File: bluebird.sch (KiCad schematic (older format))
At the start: 17 parts

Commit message: Add and wire key matrix, IO expander
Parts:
- added R? (x2): 10k, symbol Device:R
- added U2: MCP23017_SS, Package_SO:SSOP-28_5.3x10.2mm_P0.65mm, symbol Interface_Expansion:MCP23017_SS
- U1: renamed from U?; footprint (none) -> Package_QFP:TQFP-44_10x10mm_P0.8mm
- gave numbers to parts that had none: 15
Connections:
- net labels added: I2C_SCL, I2C_SDA, SPI_MISO, SPI_MOSI, SPI_SCK, col_0, col_1, col_10, col_11, col_12, col_13, col_14, col_15, col_2, col_3, col_4, col_5, col_6, col_7, col_8, col_9, row_0, row_1, row_2, row_3, row_4, row_5, ~MAIN_RST
- net labels removed: BLE_MISO, BLE_MOSI, BLE_SCK
- wire segments 88 -> 131
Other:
- moved on the sheet: C6, C7, C8, R1, R2, R3, R4, SW1, U1

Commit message: Add LED controller + LEDS
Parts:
- added C10: 0.1u, symbol Device:C_Small
- added C9: 0.22u, symbol Device:C_Small
- added R7: 20k, symbol Device:R
- added U3: IS31FL3731-SA, Package_SO:SSOP-28_5.3x10.2mm_P0.65mm, symbol Driver_LED:IS31FL3731-SA
- A1: footprint (none) -> bluebird:BLUEFRUIT_SPI_FRIEND
- gave numbers to parts that had none: 2
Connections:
- net labels added: LED_AUD_IN, LED_CA1, LED_CA2, LED_CA3, LED_CA4, LED_CA5, LED_CA6, LED_CA7, LED_CA8, LED_CA9, LED_CB1, LED_CB2, LED_CB3, LED_CB4, LED_CB5, LED_CB6, LED_CB7, LED_CB8, LED_CB9, LED_INT, LED_SHDN, col0, col1, col10, col11, col12, col13, col14, col15, col2, col3, col4, col5, col6, col7, col8, col9, row0, row1, row2, row3, row4, row5
- net labels removed: col_0, col_1, col_10, col_11, col_12, col_13, col_14, col_15, col_2, col_3, col_4, col_5, col_6, col_7, col_8, col_9, row_0, row_1, row_2, row_3, row_4, row_5
- wire segments 131 -> 166

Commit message: Finish charge controller, finish layout
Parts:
- removed X1: XTAL_GND, symbol keyboard_parts:XTAL_GND
- added C11: 1u, Capacitor_SMD:C_0805_2012Metric_Pad1.15x1.40mm_HandSolder, symbol Device:C_Small
- added C12: 0.1u, Capacitor_SMD:C_0805_2012Metric_Pad1.15x1.40mm_HandSolder, symbol Device:C_Small
- added J3: Conn_01x07, Connector_PinHeader_2.54mm:PinHeader_1x07_P2.54mm_Vertical, symbol Connector_Generic:Conn_01x07
- added Y1: FA328 16MHz, Crystal:Crystal_SMD_SeikoEpson_FA238-4Pin_3.2x2.5mm_HandSoldering, symbol Device:Crystal_GND24
- C1, C10, C2, C3, C4, C6, C7, C8, C9: footprint (none) -> Capacitor_SMD:C_0805_2012Metric_Pad1.15x1.40mm_HandSolder
- C5: value 0.1u -> 4.7u; footprint (none) -> Capacitor_SMD:C_0805_2012Metric_Pad1.15x1.40mm_HandSolder
- J1: footprint (none) -> Connector_USB:USB_C_Receptacle_GCT_USB4085
- R1, R2, R3, R4, R5, R6, R7: footprint (none) -> Resistor_SMD:R_0805_2012Metric_Pad1.15x1.40mm_HandSolder
- SW1: footprint (none) -> Button_Switch_SMD:SW_SPST_TL3342
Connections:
- net labels added: VBAT, VCC_BAT, VUSB
- wire segments 166 -> 181
- no-connect marks 0 -> 17
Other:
- moved on the sheet: A1, C1, C10, C2, C3, C4, C5, C9, J1, R1, R7, SW1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

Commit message: Route switches
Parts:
- removed J3: Conn_01x07, Connector_PinHeader_2.54mm:PinHeader_1x07_P2.54mm_Vertical, symbol Connector_Generic:Conn_01x07
- added J3: Conn_01x05, Connector_PinHeader_2.54mm:PinHeader_1x05_P2.54mm_Vertical, symbol Connector_Generic:Conn_01x05
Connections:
- wire segments 181 -> 179
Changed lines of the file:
@@
 Wire Wire Line
 	9300 2400 9400 2400
-Text GLabel 2050 4750 2    50   Input ~ 0
-BLE_DFU
-Text GLabel 2050 4850 2    50   Input ~ 0
-LED_AUD_IN
 $Comp
 L power:GND #PWR0107
@@
 Text GLabel 2050 5150 2    50   Input ~ 0
 VCC_BAT
-$Comp
-L Connector_Generic:Conn_01x07 J3
-U 1 1 6355AB09
-P 1650 5050
-F 0 "J3" H 1568 4525 50  0000 C CNN
-F 1 "Conn_01x07" H 1568 4616 50  0000 C CNN
-F 2 "Connector_PinHeader_2.54mm:PinHeader_1x07_P2.54mm_Vertical" H 1650 5050 50  0001 C CNN
-F 3 "~" H 1650 5050 50  0001 C CNN
-	1    1650 5050
-	-1   0    0    1
-$EndComp
-Wire Wire Line
-	1850 4750 2050 4750
-Wire Wire Line
-	1850 4850 2050 4850
 Wire Wire Line
 	1850 4950 2050 4950
@@
 Wire Wire Line
 	1850 5350 2050 5350
+$Comp
+L Connector_Generic:Conn_01x05 J3
+U 1 1 5E871C97
+P 1650 5150
+F 0 "J3" H 1568 4725 50  0000 C CNN
+F 1 "Conn_01x05" H 1568 4816 50  0000 C CNN
+F 2 "Connector_PinHeader_2.54mm:PinHeader_1x05_P2.54mm_Vertical" H 1650 5150 50  0001 C CNN
+F 3 "~" H 1650 5150 50  0001 C CNN
+	1    1650 5150
+	-1   0    0    1
+$EndComp
 $EndSCHEMATC

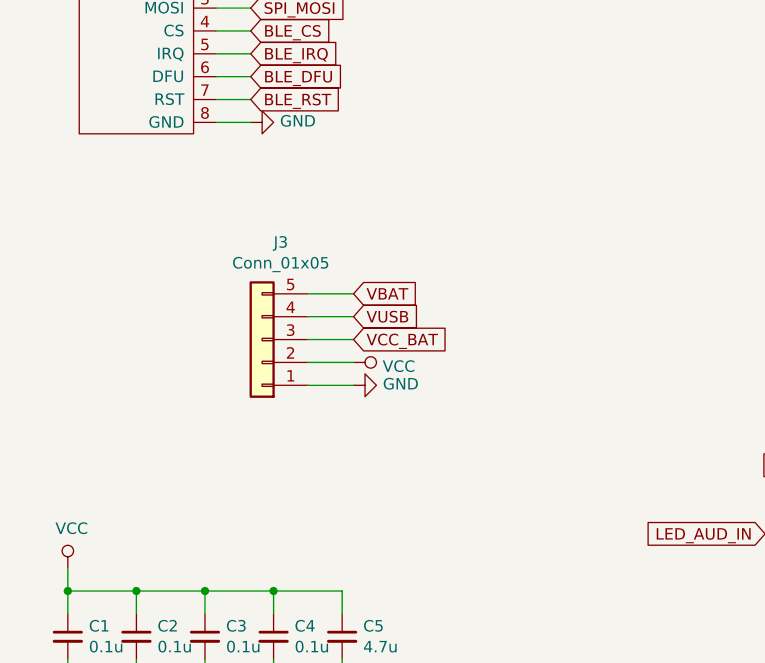
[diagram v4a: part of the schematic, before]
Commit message: Rewire as 4 layer board
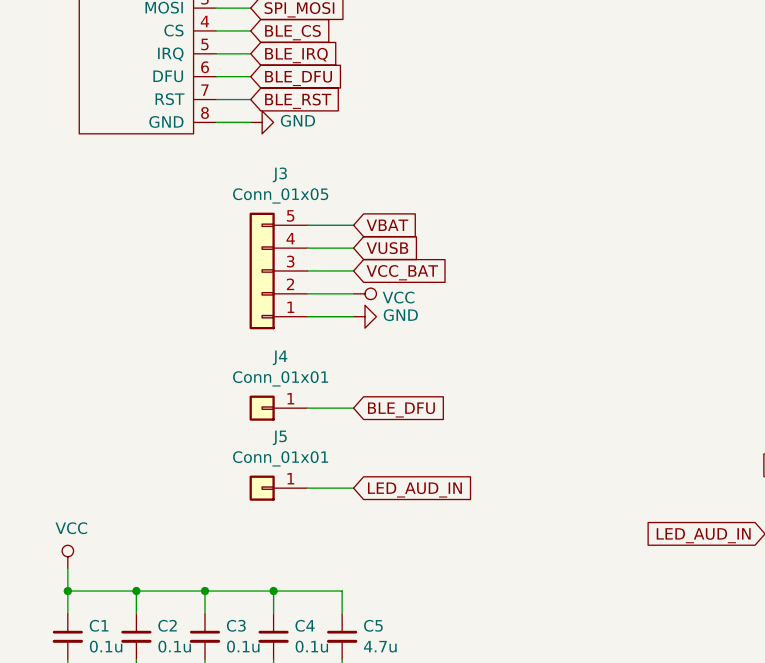
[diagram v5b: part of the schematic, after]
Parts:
- added J4, J5: Conn_01x01, Connector_PinHeader_2.54mm:PinHeader_1x01_P2.54mm_Vertical, symbol Connector_Generic:Conn_01x01
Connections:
- net BLE_DFU: now also J4.1 (Pin_1)
- net LED_AUD_IN: now also J5.1 (Pin_1)
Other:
- moved on the sheet: J3
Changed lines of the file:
@@
 L power:GND #PWR0107
 U 1 1 6354D201
-P 2050 5350
-F 0 "#PWR0107" H 2050 5100 50  0001 C CNN
-F 1 "GND" V 2055 5222 50  0000 R CNN
-F 2 "" H 2050 5350 50  0001 C CNN
-F 3 "" H 2050 5350 50  0001 C CNN
-	1    2050 5350
+P 2050 5050
+F 0 "#PWR0107" H 2050 4800 50  0001 C CNN
+F 1 "GND" V 2055 4922 50  0000 R CNN
+F 2 "" H 2050 5050 50  0001 C CNN
+F 3 "" H 2050 5050 50  0001 C CNN
+	1    2050 5050
 	0    -1   -1   0
 $EndComp
@@
 L power:VCC #PWR0108
 U 1 1 6354DC23
-P 2050 5250
-F 0 "#PWR0108" H 2050 5100 50  0001 C CNN
-F 1 "VCC" V 2068 5377 50  0000 L CNN
-F 2 "" H 2050 5250 50  0001 C CNN
-F 3 "" H 2050 5250 50  0001 C CNN
-	1    2050 5250
+P 2050 4950
+F 0 "#PWR0108" H 2050 4800 50  0001 C CNN
+F 1 "VCC" V 2068 5077 50  0000 L CNN
+F 2 "" H 2050 4950 50  0001 C CNN
+F 3 "" H 2050 4950 50  0001 C CNN
+	1    2050 4950
 	0    1    1    0
 $EndComp
-Text GLabel 2050 5050 2    50   Input ~ 0
+Text GLabel 2050 4750 2    50   Input ~ 0
 VUSB
-Text GLabel 2050 4950 2    50   Input ~ 0
+Text GLabel 2050 4650 2    50   Input ~ 0
 VBAT
-Text GLabel 2050 5150 2    50   Input ~ 0
+Text GLabel 2050 4850 2    50   Input ~ 0
 VCC_BAT
+Wire Wire Line
+	1850 4650 2050 4650
+Wire Wire Line
+	1850 4750 2050 4750
+Wire Wire Line
+	1850 4850 2050 4850
 Wire Wire Line
 	1850 4950 2050 4950
 Wire Wire Line
 	1850 5050 2050 5050
-Wire Wire Line
-	1850 5150 2050 5150
-Wire Wire Line
-	1850 5250 2050 5250
-Wire Wire Line
-	1850 5350 2050 5350
 $Comp
 L Connector_Generic:Conn_01x05 J3
 U 1 1 5E871C97
-P 1650 5150
-F 0 "J3" H 1568 4725 50  0000 C CNN
-F 1 "Conn_01x05" H 1568 4816 50  0000 C CNN
-F 2 "Connector_PinHeader_2.54mm:PinHeader_1x05_P2.54mm_Vertical" H 1650 5150 50  0001 C CNN
-F 3 "~" H 1650 5150 50  0001 C CNN
-	1    1650 5150
+P 1650 4850
+F 0 "J3" H 1568 4425 50  0000 C CNN
+F 1 "Conn_01x05" H 1568 4516 50  0000 C CNN
+F 2 "Connector_PinHeader_2.54mm:PinHeader_1x05_P2.54mm_Vertical" H 1650 4850 50  0001 C CNN
+F 3 "~" H 1650 4850 50  0001 C CNN
+	1    1650 4850
 	-1   0    0    1
 $EndComp
+$Comp
+L Connector_Generic:Conn_01x01 J4
+U 1 1 5E9FC31F
+P 1650 5450
+F 0 "J4" H 1568 5225 50  0000 C CNN
+F 1 "Conn_01x01" H 1568 5316 50  0000 C CNN
+F 2 "Connector_PinHeader_2.54mm:PinHeader_1x01_P2.54mm_Vertical" H 1650 5450 50  0001 C CNN
+F 3 "~" H 1650 5450 50  0001 C CNN
+	1    1650 5450
+	-1   0    0    1
+$EndComp
+Text GLabel 2050 5450 2    50   Input ~ 0
+BLE_DFU
+Wire Wire Line
+	2050 5450 1850 5450
+$Comp
+L Connector_Generic:Conn_01x01 J5
+U 1 1 5EA0F98E
+P 1650 5800
+F 0 "J5" H 1568 5575 50  0000 C CNN
+F 1 "Conn_01x01" H 1568 5666 50  0000 C CNN
+F 2 "Connector_PinHeader_2.54mm:PinHeader_1x01_P2.54mm_Vertical" H 1650 5800 50  0001 C CNN
+F 3 "~" H 1650 5800 50  0001 C CNN
+	1    1650 5800
+	-1   0    0    1
+$EndComp
+Text GLabel 2050 5800 2    50   Input ~ 0
+LED_AUD_IN
+Wire Wire Line
+	1850 5800 2050 5800
 $EndSCHEMATC

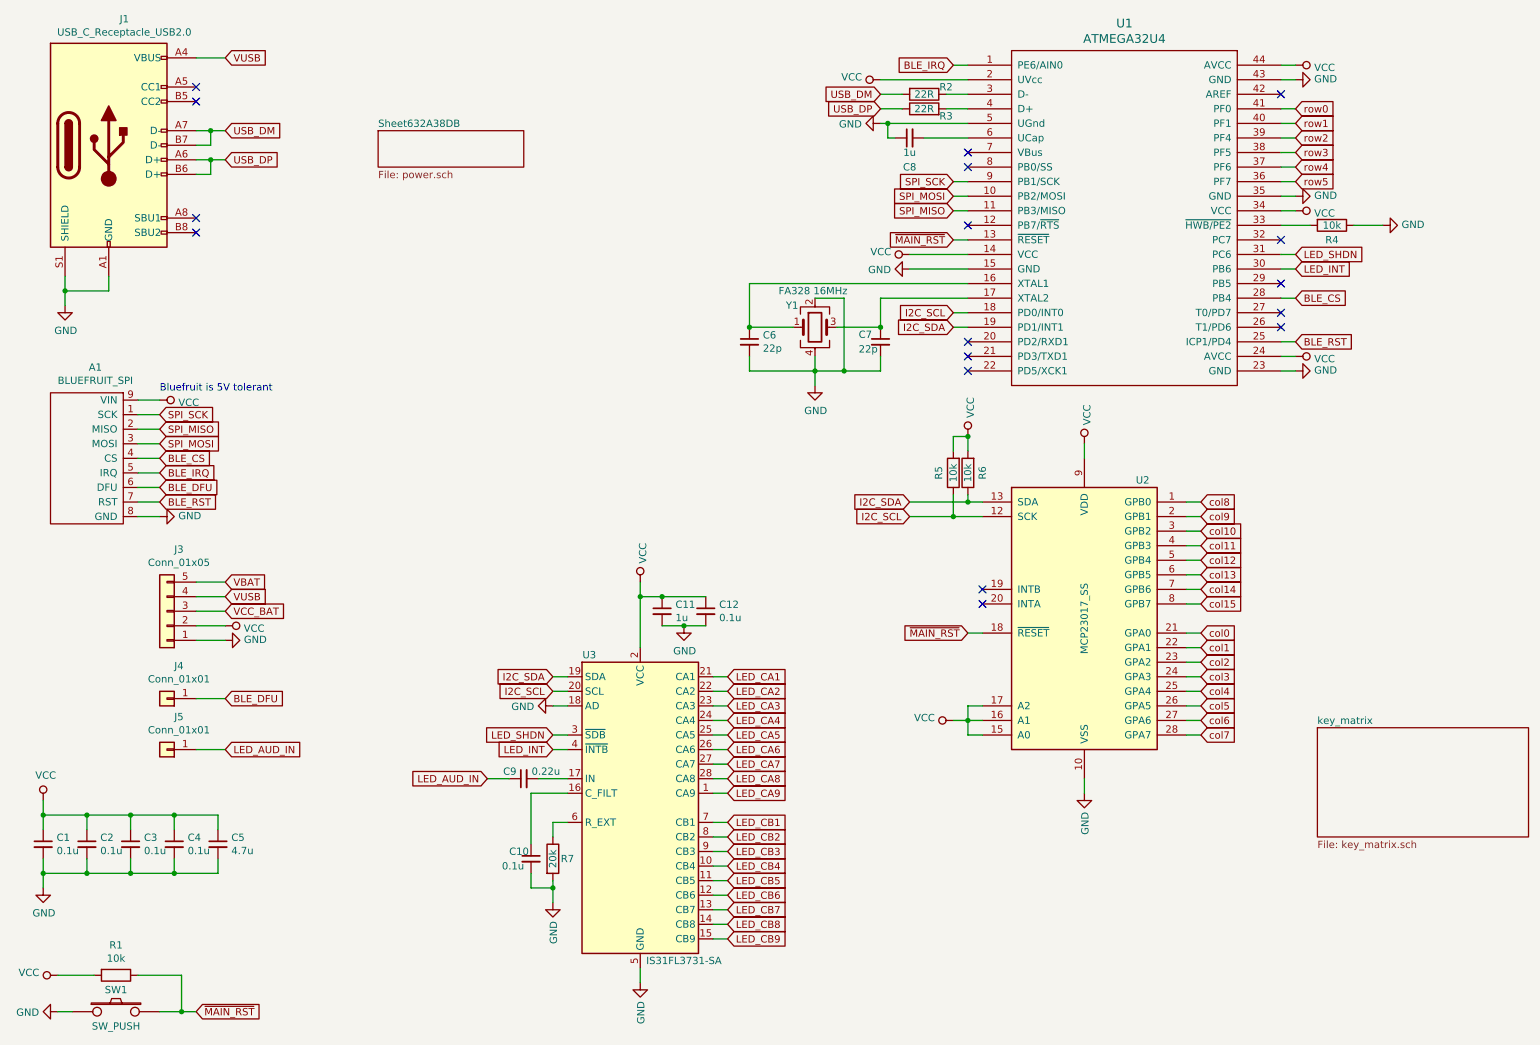
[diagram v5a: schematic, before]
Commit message: Add display and encoder
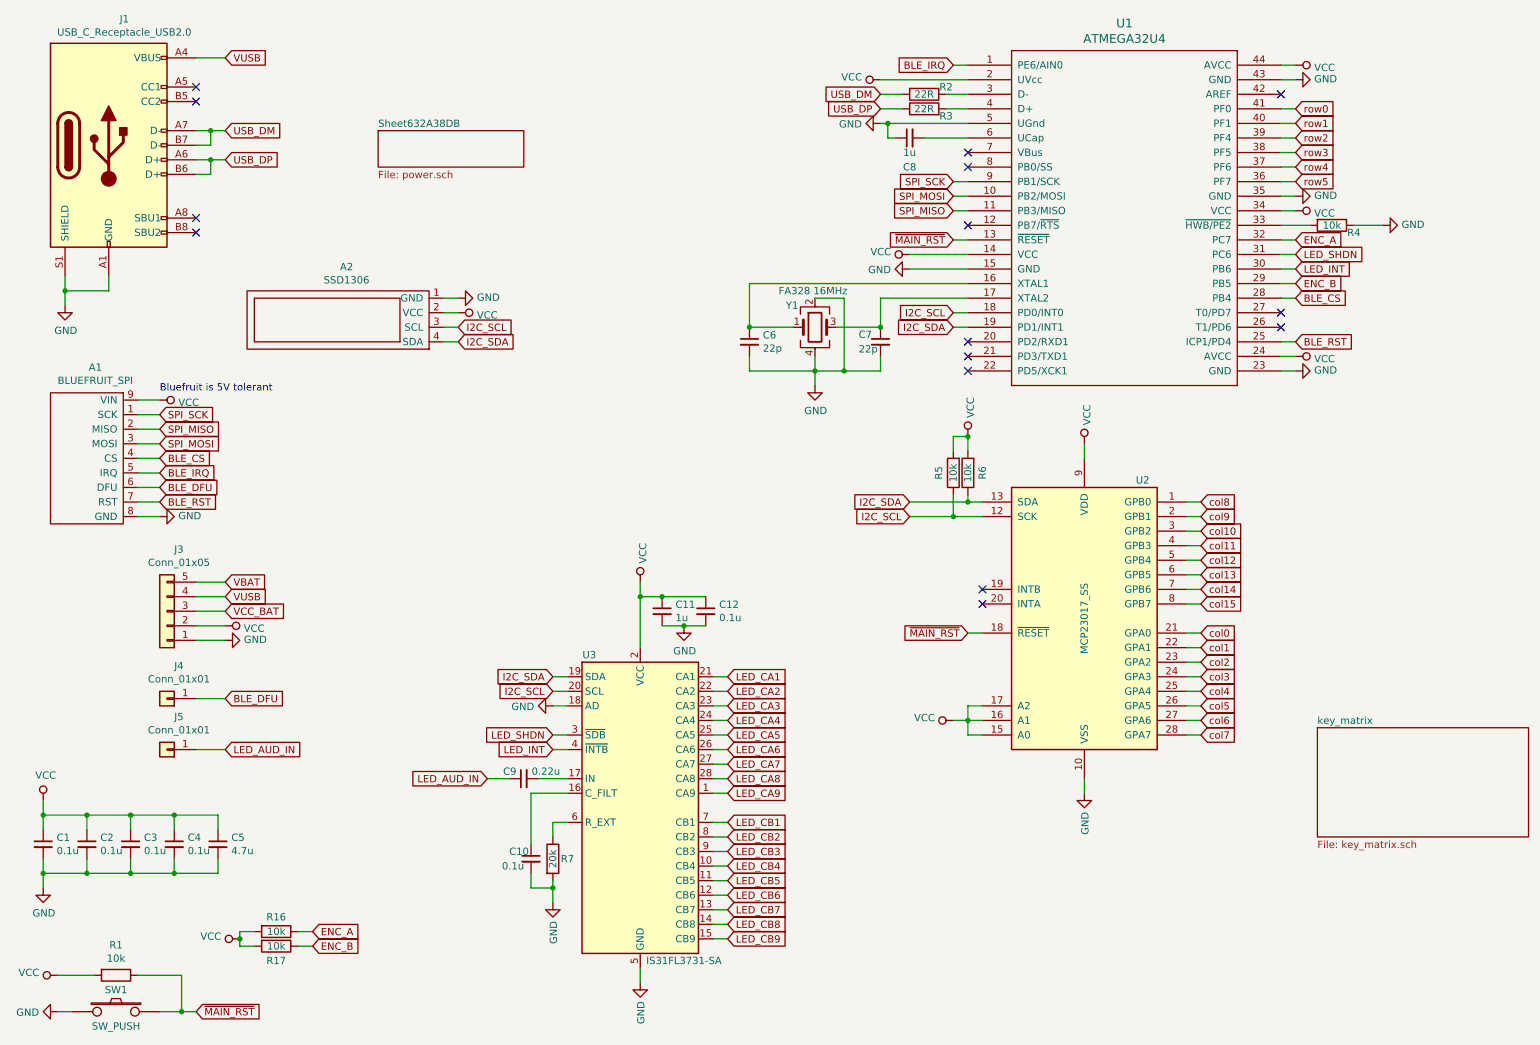
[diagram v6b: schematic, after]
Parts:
- added A2: SSD1306, bluebird:SSD1306_128x32, symbol custom:SSD1306
- added R16, R17: 10k, Resistor_SMD:R_0805_2012Metric_Pad1.15x1.40mm_HandSolder, symbol Device:R
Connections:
- net GND: now also A2.1 (GND)
- net I2C_SCL: now also A2.3 (SCL)
- net I2C_SDA: now also A2.4 (SDA)
- net VCC: now also A2.2 (VCC), R16.2, R17.2
- net ENC_B: now reaches U1.29 (PB5)
- net ENC_B: now also R17.1
- net ENC_A: now reaches U1.32 (PC7)
- net ENC_A: now also R16.1
- no-connect marks 17 -> 15
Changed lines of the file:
@@
 U 1 1 5E72BDB7
 P 9650 2200
-F 0 "R4" V 9750 2200 50  0000 C CNN
+F 0 "R4" V 9700 2350 50  0000 C CNN
 F 1 "10k" V 9650 2200 50  0000 C CNN
 F 2 "Resistor_SMD:R_0805_2012Metric_Pad1.15x1.40mm_HandSolder" V 9580 2200 50  0001 C CNN
@@
 Wire Wire Line
 	9300 1200 9400 1200
-$Comp
-L power:GND #PWR016
-U 1 1 5E74B8E7
-P 9400 2000
-F 0 "#PWR016" H 9400 1750 50  0001 C CNN
-F 1 "GND" V 9405 1872 50  0000 R CNN
-F 2 "" H 9400 2000 50  0001 C CNN
-F 3 "" H 9400 2000 50  0001 C CNN
-	1    9400 2000
-	0    -1   -1   0
-$EndComp
-$Comp
-L power:VCC #PWR017
-U 1 1 5E74C22A
-P 9400 2100
-F 0 "#PWR017" H 9400 1950 50  0001 C CNN
-F 1 "VCC" V 9417 2228 50  0000 L CNN
-F 2 "" H 9400 2100 50  0001 C CNN
-F 3 "" H 9400 2100 50  0001 C CNN
-	1    9400 2100
-	0    1    1    0
-$EndComp
-Wire Wire Line
-	9300 2000 9400 2000
-Wire Wire Line
-	9300 2100 9400 2100
 $Comp
 L power:VCC #PWR018
@@
 NoConn ~ 9300 2900
 NoConn ~ 9300 2800
-NoConn ~ 9300 2600
-NoConn ~ 9300 2300
 NoConn ~ 9300 1300
 NoConn ~ 7250 4700
@@
 Wire Wire Line
 	1850 5800 2050 5800
+$Comp
+L custom:SSD1306 A2
+U 1 1 5E76108F
+P 3450 2650
+F 0 "A2" H 4017 2485 50  0000 C CNN
+F 1 "SSD1306" H 4017 2576 50  0000 C CNN
+F 2 "bluebird:SSD1306_128x32" H 3500 2800 50  0001 C CNN
+F 3 "" H 3500 2800 50  0001 C CNN
+	1    3450 2650
+	-1   0    0    1
+$EndComp
+$Comp
+L power:VCC #PWR0109
+U 1 1 5E76A86A
+P 3650 2800
+F 0 "#PWR0109" H 3650 2650 50  0001 C CNN
+F 1 "VCC" V 3667 2928 50  0000 L CNN
+F 2 "" H 3650 2800 50  0001 C CNN
+F 3 "" H 3650 2800 50  0001 C CNN
+	1    3650 2800
+	0    1    1    0
+$EndComp
+$Comp
+L power:GND #PWR0110
+U 1 1 5E76ADAC
+P 3650 2700
+F 0 "#PWR0110" H 3650 2450 50  0001 C CNN
+F 1 "GND" V 3655 2572 50  0000 R CNN
+F 2 "" H 3650 2700 50  0001 C CNN
+F 3 "" H 3650 2700 50  0001 C CNN
+	1    3650 2700
+	0    -1   -1   0
+$EndComp
+Text GLabel 3650 3000 2    50   Input ~ 0
+I2C_SDA
+Text GLabel 3650 2900 2    50   Input ~ 0
+I2C_SCL
+Wire Wire Line
+	3550 2700 3650 2700
+Wire Wire Line
+	3550 2800 3650 2800
+Wire Wire Line
+	3550 2900 3650 2900
+Wire Wire Line
+	3550 3000 3650 3000
+Text GLabel 9400 2600 2    50   Input ~ 0
+ENC_B
+Wire Wire Line
+	9400 2600 9300 2600
+Wire Wire Line
+	9300 2300 9400 2300
+Wire Wire Line
+	9300 2100 9400 2100
+Wire Wire Line
+	9300 2000 9400 2000
+$Comp
+L power:GND #PWR016
+U 1 1 5E74B8E7
+P 9400 2000
+F 0 "#PWR016" H 9400 1750 50  0001 C CNN
+F 1 "GND" V 9405 1872 50  0000 R CNN
+F 2 "" H 9400 2000 50  0001 C CNN
+F 3 "" H 9400 2000 50  0001 C CNN
+	1    9400 2000
+	0    -1   -1   0
+$EndComp
+$Comp
+L power:VCC #PWR017
+U 1 1 5E74C22A
+P 9400 2100
+F 0 "#PWR017" H 9400 1950 50  0001 C CNN
+F 1 "VCC" V 9417 2228 50  0000 L CNN
+F 2 "" H 9400 2100 50  0001 C CNN
+F 3 "" H 9400 2100 50  0001 C CNN
+	1    9400 2100
+	0    1    1    0
+$EndComp
+Text GLabel 9400 2300 2    50   Input ~ 0
+ENC_A
+Text GLabel 2650 7050 2    50   Input ~ 0
+ENC_A
+Text GLabel 2650 7150 2    50   Input ~ 0
+ENC_B
+$Comp
+L Device:R R17
+U 1 1 5E8DE300
+P 2400 7150
+F 0 "R17" V 2500 7150 50  0000 C CNN
+F 1 "10k" V 2400 7150 50  0000 C CNN
+F 2 "Resistor_SMD:R_0805_2012Metric_Pad1.15x1.40mm_HandSolder" V 2330 7150 50  0001 C CNN
+F 3 "~" H 2400 7150 50  0001 C CNN
+	1    2400 7150
+	0    1    1    0
+$EndComp
+$Comp
+L Device:R R16
+U 1 1 5E8DE874
+P 2400 7050
+F 0 "R16" V 2300 7050 50  0000 C CNN
+F 1 "10k" V 2400 7050 50  0000 C CNN
+F 2 "Resistor_SMD:R_0805_2012Metric_Pad1.15x1.40mm_HandSolder" V 2330 7050 50  0001 C CNN
+F 3 "~" H 2400 7050 50  0001 C CNN
+	1    2400 7050
+	0    1    1    0
+$EndComp
+Wire Wire Line
+	2650 7150 2550 7150
+Wire Wire Line
+	2650 7050 2550 7050
+$Comp
+L power:VCC #PWR028
+U 1 1 5E8F7EED
+P 2150 7100
+F 0 "#PWR028" H 2150 6950 50  0001 C CNN
+F 1 "VCC" V 2167 7228 50  0000 L CNN
+F 2 "" H 2150 7100 50  0001 C CNN
+F 3 "" H 2150 7100 50  0001 C CNN
+	1    2150 7100
+	0    -1   -1   0
+$EndComp
+Wire Wire Line
+	2250 7150 2150 7150
+Wire Wire Line
+	2150 7150 2150 7100
+Wire Wire Line
+	2250 7050 2150 7050
+Wire Wire Line
+	2150 7050 2150 7100
+Connection ~ 2150 7100
 $EndSCHEMATC
